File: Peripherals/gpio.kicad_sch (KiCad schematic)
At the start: 4 parts, among them J4 Pyro Connectors

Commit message: Reorganised repo
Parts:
- D4: value GREEN -> (none); footprint LED_SMD:LED_0603_1608Metric -> (none)
- F1: value 2A Poly -> (none); footprint Fuse:Fuse_0603_1608Metric -> (none)
- J4: value Pyro Connectors -> (none); footprint YAR_Connectors:ScrewTerm_2.54x10 -> (none)
- R14: value 470 -> (none); footprint Resistor_SMD:R_0603_1608Metric -> (none)
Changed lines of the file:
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@@
       (effects (font (size 1.27 1.27)) (justify left))
     )
-    (property "Value" "Pyro Connectors" (id 1) (at 40.64 100.33 0)
+    (property "Value" "" (id 1) (at 40.64 100.33 0)
       (effects (font (size 1.27 1.27)) (justify left))
     )
-    (property "Footprint" "YAR_Connectors:ScrewTerm_2.54x10" (id 2) (at 45.72 116.84 0)
+    (property "Footprint" "" (id 2) (at 45.72 116.84 0)
       (effects (font (size 1.27 1.27)) hide)
     )
@@
       (effects (font (size 1.27 1.27)) (justify left))
     )
-    (property "Value" "470" (id 1) (at 93.98 44.4499 0)
+    (property "Value" "" (id 1) (at 93.98 44.4499 0)
       (effects (font (size 1.27 1.27)) (justify left))
     )
-    (property "Footprint" "Resistor_SMD:R_0603_1608Metric" (id 2) (at 89.662 43.18 90)
+    (property "Footprint" "" (id 2) (at 89.662 43.18 90)
       (effects (font (size 1.27 1.27)) hide)
     )
@@
   (symbol (lib_id "power:GND") (at 91.44 46.99 0) (unit 1)
     (in_bom yes) (on_board yes) (fields_autoplaced)
-    (property "Reference" "#PWR070" (id 0) (at 91.44 53.34 0)
+    (property "Reference" "#PWR?" (id 0) (at 91.44 53.34 0)
       (effects (font (size 1.27 1.27)) hide)
     )
-    (property "Value" "GND" (id 1) (at 91.44 52.07 0))
+    (property "Value" "" (id 1) (at 91.44 52.07 0))
     (property "Footprint" "" (id 2) (at 91.44 46.99 0)
       (effects (font (size 1.27 1.27)) hide)
@@
     (in_bom yes) (on_board yes) (fields_autoplaced)
     (property "Reference" "F1" (id 0) (at 33.02 97.79 90))
-    (property "Value" "2A Poly" (id 1) (at 33.02 100.33 90))
-    (property "Footprint" "Fuse:Fuse_0603_1608Metric" (id 2) (at 38.1 102.87 0)
+    (property "Value" "" (id 1) (at 33.02 100.33 90))
+    (property "Footprint" "" (id 2) (at 38.1 102.87 0)
       (effects (font (size 1.27 1.27)) (justify left) hide)
     )
@@
       (effects (font (size 1.27 1.27)) (justify right))
     )
-    (property "Value" "GREEN" (id 1) (at 95.25 35.8774 90)
+    (property "Value" "" (id 1) (at 95.25 35.8774 90)
       (effects (font (size 1.27 1.27)) (justify right))
     )
-    (property "Footprint" "LED_SMD:LED_0603_1608Metric" (id 2) (at 91.44 33.02 0)
+    (property "Footprint" "" (id 2) (at 91.44 33.02 0)
       (effects (font (size 1.27 1.27)) hide)
     )
@@
   (symbol (lib_id "power:+BATT") (at 25.4 104.14 90) (unit 1)
     (in_bom yes) (on_board yes)
-    (property "Reference" "#PWR069" (id 0) (at 29.21 104.14 0)
+    (property "Reference" "#PWR?" (id 0) (at 29.21 104.14 0)
       (effects (font (size 1.27 1.27)) hide)
     )
-    (property "Value" "+BATT" (id 1) (at 16.51 104.14 90)
+    (property "Value" "" (id 1) (at 16.51 104.14 90)
       (effects (font (size 1.27 1.27)) (justify right))
     )

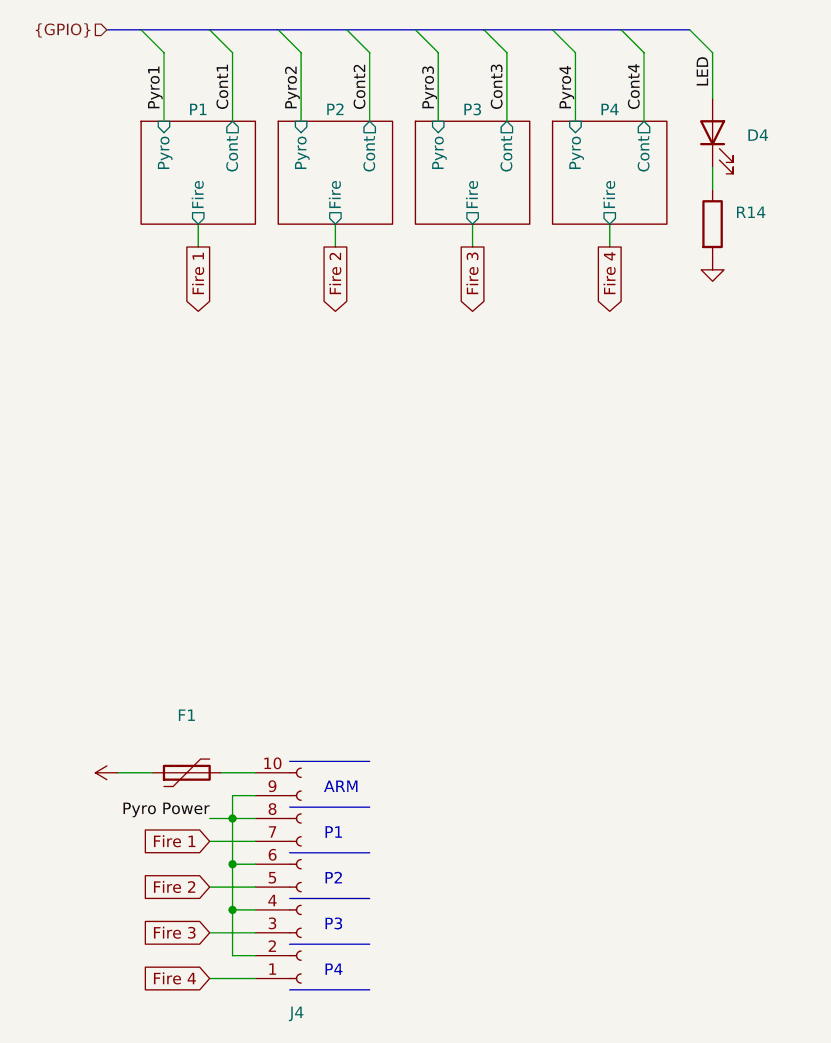
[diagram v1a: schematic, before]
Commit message: rev2 changes excluding pyro
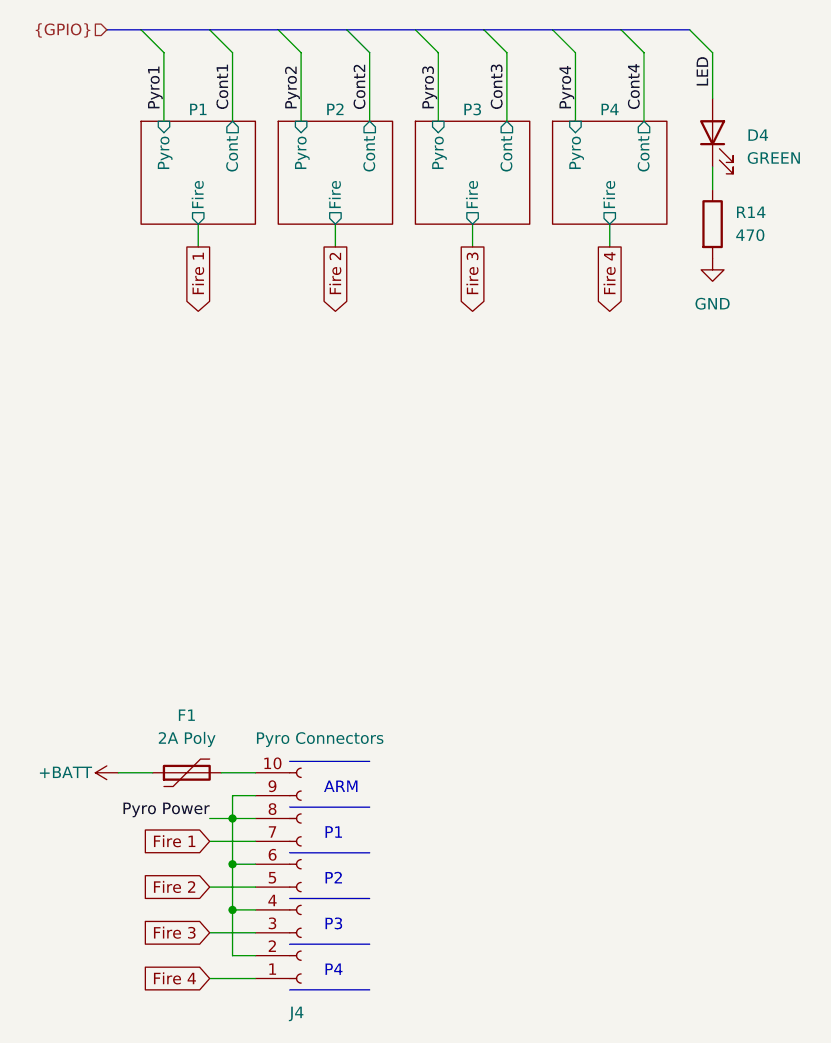
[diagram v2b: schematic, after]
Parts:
- D4: value (none) -> GREEN; footprint (none) -> LED_SMD:LED_0603_1608Metric
- F1: value (none) -> 2A Poly; footprint (none) -> Fuse:Fuse_0603_1608Metric
- J4: value (none) -> Pyro Connectors; footprint (none) -> YAR_Connectors:ScrewTerm_2.54x10
- R14: value (none) -> 470; footprint (none) -> Resistor_SMD:R_0603_1608Metric
